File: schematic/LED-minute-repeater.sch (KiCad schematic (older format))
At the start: 19 parts, among them J1 ICSP, J2 WS2812B_OUT, J3 I2C, SW2 Hour, SW3 Minute, U1 ATTiny85, U2 DS3231, U3 MCP1700T

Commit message: fix reg and RTC chip pin assign swap
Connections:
- net RTC_SCL: now also R7.2, U2.16 (SCL); no longer R1.2, U2.15 (SDA)
- net RTC_SDA: now also R1.2, U2.15 (SDA); no longer R7.2, U2.16 (SCL)
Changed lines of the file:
@@
 	1    0    0    -1
 $EndComp
+Text GLabel 7700 3150 0    60   Input ~ 0
+RTC_SDA
 Text GLabel 7700 3050 0    60   Input ~ 0
-RTC_SDA
-Text GLabel 7700 3150 0    60   Input ~ 0
 RTC_SCL
 $Comp

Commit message: PCB layout for rev 0.2 circuit
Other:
- note added: "0.2"
- note added: "2017-04-29"
- note added: "LED Minute Repeater Clock (ATtiny85)"
- note added: "[Rev 0.2]\n - Fixed MCP1700 pin assign (Vin <-> Vout)\n - Fixed DS3231 pin assign (SCL <-> SDA)"
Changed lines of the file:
@@
 	1    0    0    -1
 $EndComp
+Text Notes 8150 7650 0    60   ~ 0
+2017-04-29
+Text Notes 7350 7500 0    60   ~ 0
+LED Minute Repeater Clock (ATtiny85)
+Text Notes 10550 7650 0    60   ~ 0
+0.2
+Text Notes 7000 6750 0    40   ~ 0
+[Rev 0.2]\n  - Fixed MCP1700 pin assign (Vin <-> Vout)\n  - Fixed DS3231 pin assign (SCL <-> SDA)
 $EndSCHEMATC

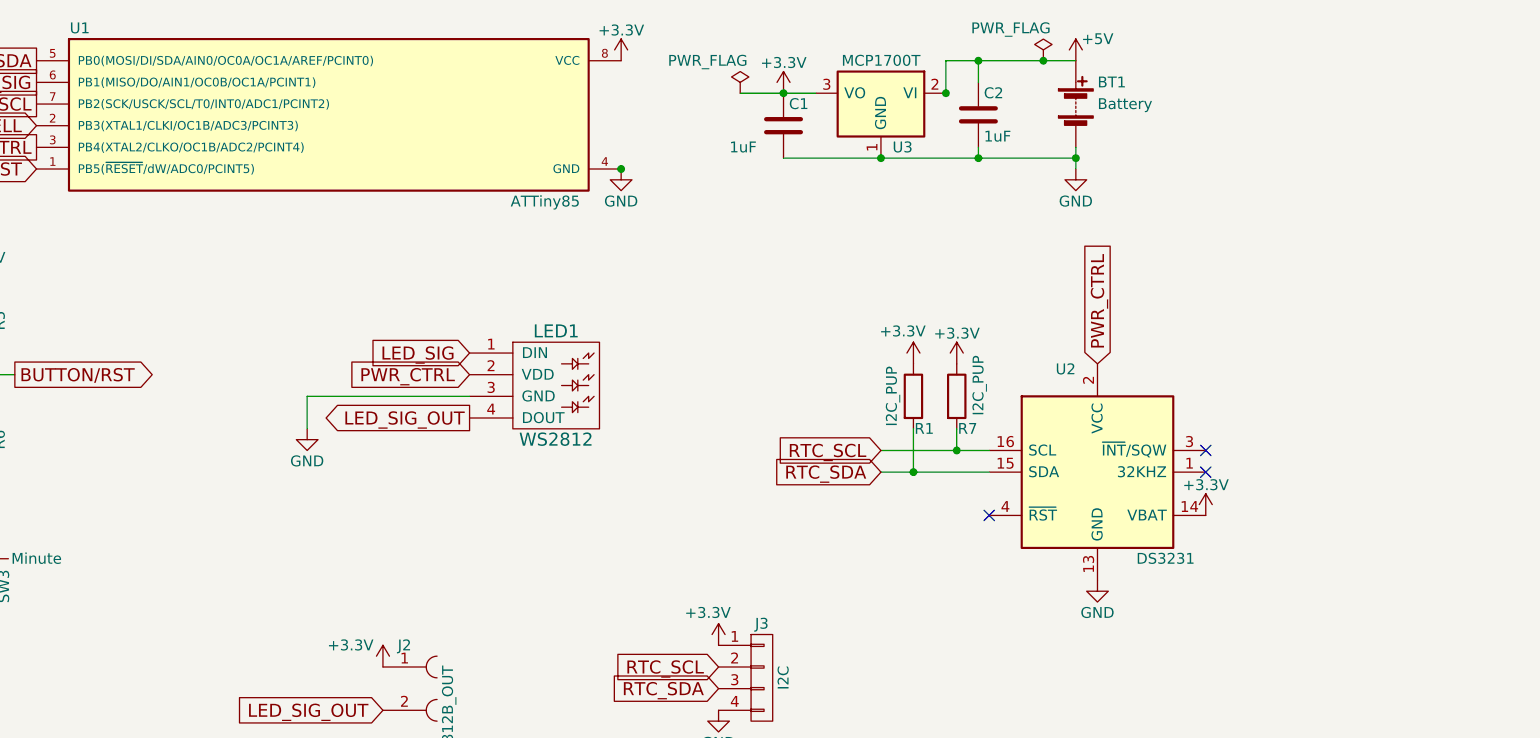
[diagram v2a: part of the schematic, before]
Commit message: Smaller size SMD version of PCB
OSH Order #MdFUZar9
Erratta:
    - I2C GND is not connected
    - Reg (MCP1700) GND is not connected
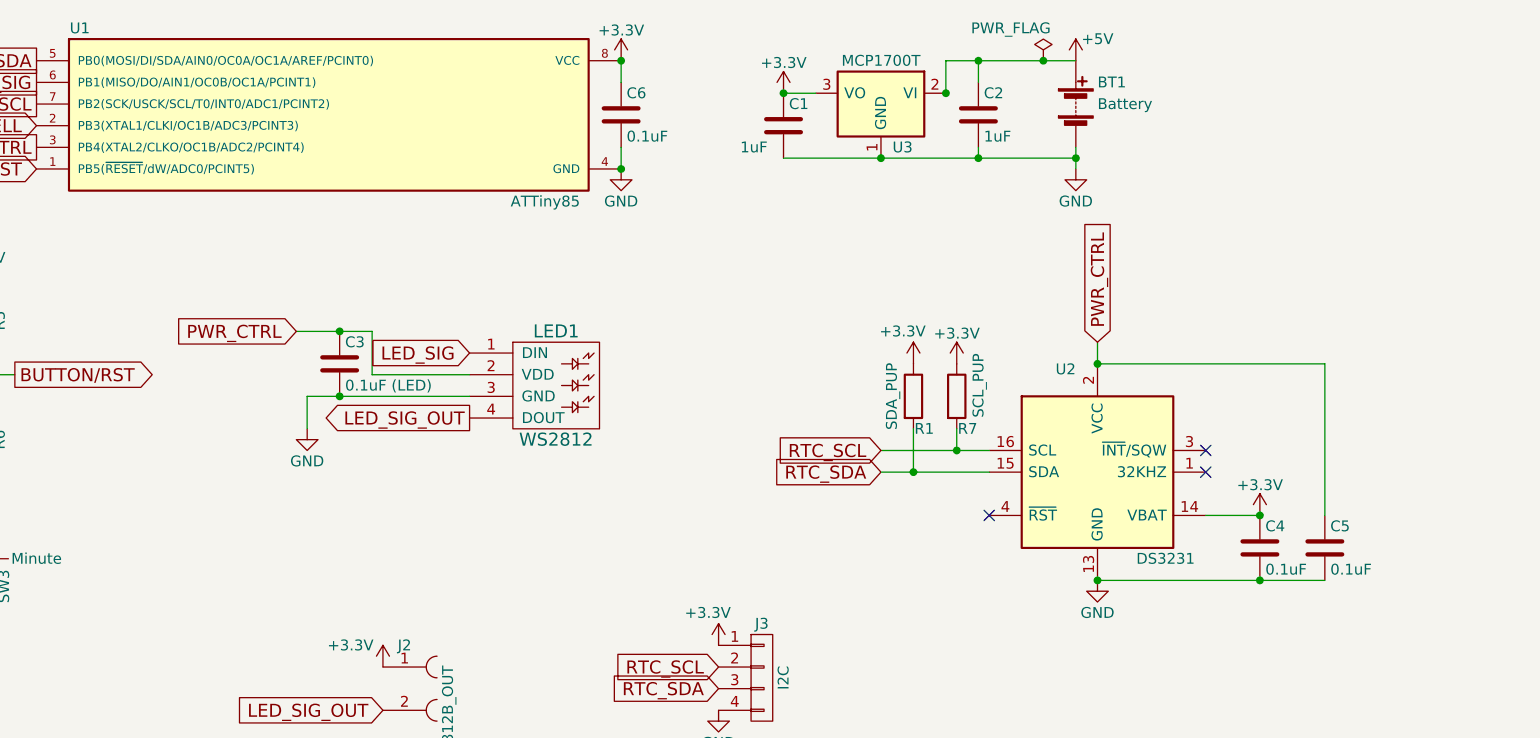
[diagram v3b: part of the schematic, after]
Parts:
- added C3: 0.1uF (LED), Capacitors_SMD:C_0805_HandSoldering, symbol C
- added C4, C5, C6: 0.1uF, Capacitors_SMD:C_0805_HandSoldering, symbol C
- C1, C2: footprint Capacitors_THT:C_Disc_D3.0mm_W1.6mm_P2.50mm -> Capacitors_SMD:C_0805_HandSoldering
- R1: value I2C_PUP -> SDA_PUP; footprint Resistors_THT:R_Axial_DIN0204_L3.6mm_D1.6mm_P7.62mm_Horizontal -> Resistors_SMD:R_0805_HandSoldering
- R3, R4, R5, R6: footprint Resistors_THT:R_Axial_DIN0204_L3.6mm_D1.6mm_P7.62mm_Horizontal -> Resistors_SMD:R_0805_HandSoldering
- R7: value I2C_PUP -> SCL_PUP; footprint Resistors_THT:R_Axial_DIN0204_L3.6mm_D1.6mm_P7.62mm_Horizontal -> Resistors_SMD:R_0805_HandSoldering
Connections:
- net +3V3: now also C4.1, C6.1
- net GND: now also C3.2, C4.2, C5.2, C6.2
- net PWR_CTRL: now also C3.1, C5.1
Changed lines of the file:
@@
 F 0 "R3" V 2330 2600 50  0000 C CNN
 F 1 "R_ADC" V 2150 2600 50  0000 C CNN
-F 2 "Resistors_THT:R_Axial_DIN0204_L3.6mm_D1.6mm_P7.62mm_Horizontal" V 2180 2600 50  0001 C CNN
+F 2 "Resistors_SMD:R_0805_HandSoldering" V 2180 2600 50  0001 C CNN
 F 3 "" H 2250 2600 50  0001 C CNN
 	1    2250 2600
@@
 F 0 "R4" V 3230 3000 50  0000 C CNN
 F 1 "10K" V 3150 3000 50  0000 C CNN
-F 2 "Resistors_THT:R_Axial_DIN0204_L3.6mm_D1.6mm_P7.62mm_Horizontal" V 3080 3000 50  0001 C CNN
+F 2 "Resistors_SMD:R_0805_HandSoldering" V 3080 3000 50  0001 C CNN
 F 3 "" H 3150 3000 50  0001 C CNN
 	1    3150 3000
@@
 Text GLabel 2250 2000 0    60   Input ~ 0
 PWR_CTRL
-Text GLabel 5800 2700 0    60   Input ~ 0
+Text GLabel 5000 2500 0    60   Input ~ 0
 PWR_CTRL
 Text GLabel 3800 1350 0    60   Output ~ 0
@@
 L +3.3V #PWR05
 U 1 1 58D440B9
-P 9200 3350
-F 0 "#PWR05" H 9200 3200 50  0001 C CNN
-F 1 "+3.3V" H 9200 3490 50  0000 C CNN
-F 2 "" H 9200 3350 50  0001 C CNN
-F 3 "" H 9200 3350 50  0001 C CNN
-	1    9200 3350
+P 9450 3350
+F 0 "#PWR05" H 9450 3200 50  0001 C CNN
+F 1 "+3.3V" H 9450 3490 50  0000 C CNN
+F 2 "" H 9450 3350 50  0001 C CNN
+F 3 "" H 9450 3350 50  0001 C CNN
+	1    9450 3350
 	1    0    0    -1
 $EndComp
@@
 F 0 "R6" V 3630 3000 50  0000 C CNN
 F 1 "5K" V 3550 3000 50  0000 C CNN
-F 2 "Resistors_THT:R_Axial_DIN0204_L3.6mm_D1.6mm_P7.62mm_Horizontal" V 3480 3000 50  0001 C CNN
+F 2 "Resistors_SMD:R_0805_HandSoldering" V 3480 3000 50  0001 C CNN
 F 3 "" H 3550 3000 50  0001 C CNN
 	1    3550 3000
@@
 F 0 "R5" V 3630 2450 50  0000 C CNN
 F 1 "2K" V 3550 2450 50  0000 C CNN
-F 2 "Resistors_THT:R_Axial_DIN0204_L3.6mm_D1.6mm_P7.62mm_Horizontal" V 3480 2450 50  0001 C CNN
+F 2 "Resistors_SMD:R_0805_HandSoldering" V 3480 2450 50  0001 C CNN
 F 3 "" H 3550 2450 50  0001 C CNN
 	1    3550 2450
@@
 	1    0    0    -1
 $EndComp
-Text GLabel 8700 2650 1    60   Input ~ 0
+Text GLabel 8700 2550 1    60   Input ~ 0
 PWR_CTRL
 $Comp
@@
 F 0 "C2" H 8175 1600 50  0000 L CNN
 F 1 "1uF" H 8175 1400 50  0000 L CNN
-F 2 "Capacitors_THT:C_Disc_D3.0mm_W1.6mm_P2.50mm" H 8188 1350 50  0001 C CNN
+F 2 "Capacitors_SMD:C_0805_HandSoldering" H 8188 1350 50  0001 C CNN
 F 3 "" H 8150 1500 50  0001 C CNN
 	1    8150 1500
@@
 P 7250 1550
 F 0 "C1" H 7275 1650 50  0000 L CNN
-F 1 "1uF" H 7000 1450 50  0000 L CNN
-F 2 "Capacitors_THT:C_Disc_D3.0mm_W1.6mm_P2.50mm" H 7288 1400 50  0001 C CNN
+F 1 "1uF" H 7050 1450 50  0000 L CNN
+F 2 "Capacitors_SMD:C_0805_HandSoldering" H 7288 1400 50  0001 C CNN
 F 3 "" H 7250 1550 50  0001 C CNN
 	1    7250 1550
@@
 P 8050 2800
 F 0 "R7" H 8100 2650 50  0000 C CNN
-F 1 "I2C_PUP" V 8150 2850 50  0000 C CNN
-F 2 "Resistors_THT:R_Axial_DIN0204_L3.6mm_D1.6mm_P7.62mm_Horizontal" V 7980 2800 50  0001 C CNN
+F 1 "SCL_PUP" V 8150 2850 50  0000 C CNN
+F 2 "Resistors_SMD:R_0805_HandSoldering" V 7980 2800 50  0001 C CNN
 F 3 "" H 8050 2800 50  0001 C CNN
 	1    8050 2800
@@
 P 7850 2800
 F 0 "R1" H 7900 2650 50  0000 C CNN
-F 1 "I2C_PUP" V 7750 2800 50  0000 C CNN
-F 2 "Resistors_THT:R_Axial_DIN0204_L3.6mm_D1.6mm_P7.62mm_Horizontal" V 7780 2800 50  0001 C CNN
+F 1 "SDA_PUP" V 7750 2800 50  0000 C CNN
+F 2 "Resistors_SMD:R_0805_HandSoldering" V 7780 2800 50  0001 C CNN
 F 3 "" H 7850 2800 50  0001 C CNN
 	1    7850 2800
@@
 	1    0    0    -1
 $EndComp
-Wire Wire Line
-	2250 2450 2650 2450
-Connection ~ 2250 2450
-Wire Wire Line
-	3550 2600 3550 2850
-Wire Wire Line
-	3550 2850 3150 2850
-Wire Wire Line
-	3550 2700 3700 2700
-Connection ~ 3550 2700
-Wire Wire Line
-	3550 3150 3550 3350
-Wire Wire Line
-	3150 3150 3150 3350
-Wire Wire Line
-	3150 3750 3150 3950
-Wire Wire Line
-	3150 3950 3550 3950
-Wire Wire Line
-	3550 3950 3550 3750
-Wire Wire Line
-	2250 2000 2250 2150
-Wire Wire Line
-	2250 2750 2250 2900
-Connection ~ 3350 3950
-Wire Wire Line
-	7250 1700 8600 1700
-Wire Wire Line
-	8000 1250 8600 1250
-Wire Wire Line
-	8000 1250 8000 1400
-Wire Wire Line
-	8150 1250 8150 1350
-Connection ~ 8150 1250
-Wire Wire Line
-	8150 1700 8150 1650
-Connection ~ 8150 1700
-Connection ~ 7700 1700
-Wire Wire Line
-	7050 1400 7400 1400
-Connection ~ 7250 1400
-Wire Wire Line
-	7700 3050 8200 3050
-Wire Wire Line
-	7700 3150 8200 3150
-Wire Wire Line
-	7850 2950 7850 3150
-Connection ~ 7850 3150
-Wire Wire Line
-	8050 2950 8050 3050
-Connection ~ 8050 3050
-Wire Wire Line
-	8600 1650 8600 1750
-Connection ~ 8600 1700
 $Comp
 L WS2812 LED1
@@
 	1    0    0    -1
 $EndComp
-Wire Wire Line
-	5050 2950 5050 2800
-Wire Wire Line
-	5050 2800 5800 2800
-Connection ~ 6500 1750
-Connection ~ 8000 1400
-Connection ~ 8450 1250
-$Comp
-L PWR_FLAG #FLG021
-U 1 1 58EF1A94
-P 7050 1400
-F 0 "#FLG021" H 7050 1475 50  0001 C CNN
-F 1 "PWR_FLAG" H 6900 1550 50  0000 C CNN
-F 2 "" H 7050 1400 50  0001 C CNN
-F 3 "" H 7050 1400 50  0001 C CNN
-	1    7050 1400
-	1    0    0    -1
-$EndComp
 Text Notes 8150 7650 0    60   ~ 0
 2017-04-29
@@
 Text Notes 7000 6750 0    40   ~ 0
 [Rev 0.2]\n  - Fixed MCP1700 pin assign (Vin <-> Vout)\n  - Fixed DS3231 pin assign (SCL <-> SDA)
+$Comp
+L C C4
+U 1 1 59052A27
+P 9450 3500
+F 0 "C4" H 9475 3600 50  0000 L CNN
+F 1 "0.1uF" H 9475 3400 50  0000 L CNN
+F 2 "Capacitors_SMD:C_0805_HandSoldering" H 9488 3350 50  0001 C CNN
+F 3 "" H 9450 3500 50  0001 C CNN
+	1    9450 3500
+	1    0    0    -1
+$EndComp
+$Comp
+L C C5
+U 1 1 59052ACC
+P 9750 3500
+F 0 "C5" H 9775 3600 50  0000 L CNN
+F 1 "0.1uF" H 9775 3400 50  0000 L CNN
+F 2 "Capacitors_SMD:C_0805_HandSoldering" H 9788 3350 50  0001 C CNN
+F 3 "" H 9750 3500 50  0001 C CNN
+	1    9750 3500
+	1    0    0    -1
+$EndComp
+$Comp
+L C C6
+U 1 1 59054059
+P 6500 1500
+F 0 "C6" H 6525 1600 50  0000 L CNN
+F 1 "0.1uF" H 6525 1400 50  0000 L CNN
+F 2 "Capacitors_SMD:C_0805_HandSoldering" H 6538 1350 50  0001 C CNN
+F 3 "" H 6500 1500 50  0001 C CNN
+	1    6500 1500
+	1    0    0    -1
+$EndComp
+$Comp
+L C C3
+U 1 1 590540B2
+P 5200 2650
+F 0 "C3" H 5225 2750 50  0000 L CNN
+F 1 "0.1uF (LED)" H 5225 2550 50  0000 L CNN
+F 2 "Capacitors_SMD:C_0805_HandSoldering" H 5238 2500 50  0001 C CNN
+F 3 "" H 5200 2650 50  0001 C CNN
+	1    5200 2650
+	1    0    0    -1
+$EndComp
+Wire Wire Line
+	2250 2450 2650 2450
+Connection ~ 2250 2450
+Wire Wire Line
+	3550 2600 3550 2850
+Wire Wire Line
+	3550 2850 3150 2850
+Wire Wire Line
+	3550 2700 3700 2700
+Connection ~ 3550 2700
+Wire Wire Line
+	3550 3150 3550 3350
+Wire Wire Line
+	3150 3150 3150 3350
+Wire Wire Line
+	3150 3750 3150 3950
+Wire Wire Line
+	3150 3950 3550 3950
+Wire Wire Line
+	3550 3950 3550 3750
+Wire Wire Line
+	2250 2000 2250 2150
+Wire Wire Line
+	2250 2750 2250 2900
+Connection ~ 3350 3950
+Wire Wire Line
+	7250 1700 8600 1700
+Wire Wire Line
+	8000 1250 8600 1250
+Wire Wire Line
+	8000 1250 8000 1400
+Wire Wire Line
+	8150 1250 8150 1350
+Connection ~ 8150 1250
+Wire Wire Line
+	8150 1700 8150 1650
+Connection ~ 8150 1700
+Connection ~ 7700 1700
+Wire Wire Line
+	7250 1400 7400 1400
+Connection ~ 7250 1400
+Wire Wire Line
+	7700 3050 8200 3050
+Wire Wire Line
+	7700 3150 8200 3150
+Wire Wire Line
+	7850 2950 7850 3150
+Connection ~ 7850 3150
+Wire Wire Line
+	8050 2950 8050 3050
+Connection ~ 8050 3050
+Wire Wire Line
+	8600 1650 8600 1750
+Connection ~ 8600 1700
+Wire Wire Line
+	5050 2950 5050 2800
+Connection ~ 6500 1750
+Connection ~ 8000 1400
+Connection ~ 8450 1250
+Wire Wire Line
+	5350 2500 5350 2700
+Wire Wire Line
+	5350 2700 5800 2700
+Wire Wire Line
+	8700 3650 9750 3650
+Connection ~ 9450 3650
+Wire Wire Line
+	9200 3350 9450 3350
+Wire Wire Line
+	8700 2550 8700 2650
+Wire Wire Line
+	8700 2650 9750 2650
+Wire Wire Line
+	9750 2650 9750 3350
+Connection ~ 6500 1250
+Connection ~ 9450 3350
+Connection ~ 8700 3650
+Connection ~ 8700 2650
+Wire Wire Line
+	6500 1250 6500 1350
+Wire Wire Line
+	6500 1650 6500 1750
+Connection ~ 5200 2800
+Wire Wire Line
+	5050 2800 5800 2800
+Wire Wire Line
+	5000 2500 5350 2500
+Connection ~ 5200 2500
 $EndSCHEMATC
